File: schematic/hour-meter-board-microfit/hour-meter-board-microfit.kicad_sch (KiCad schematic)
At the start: 0 parts

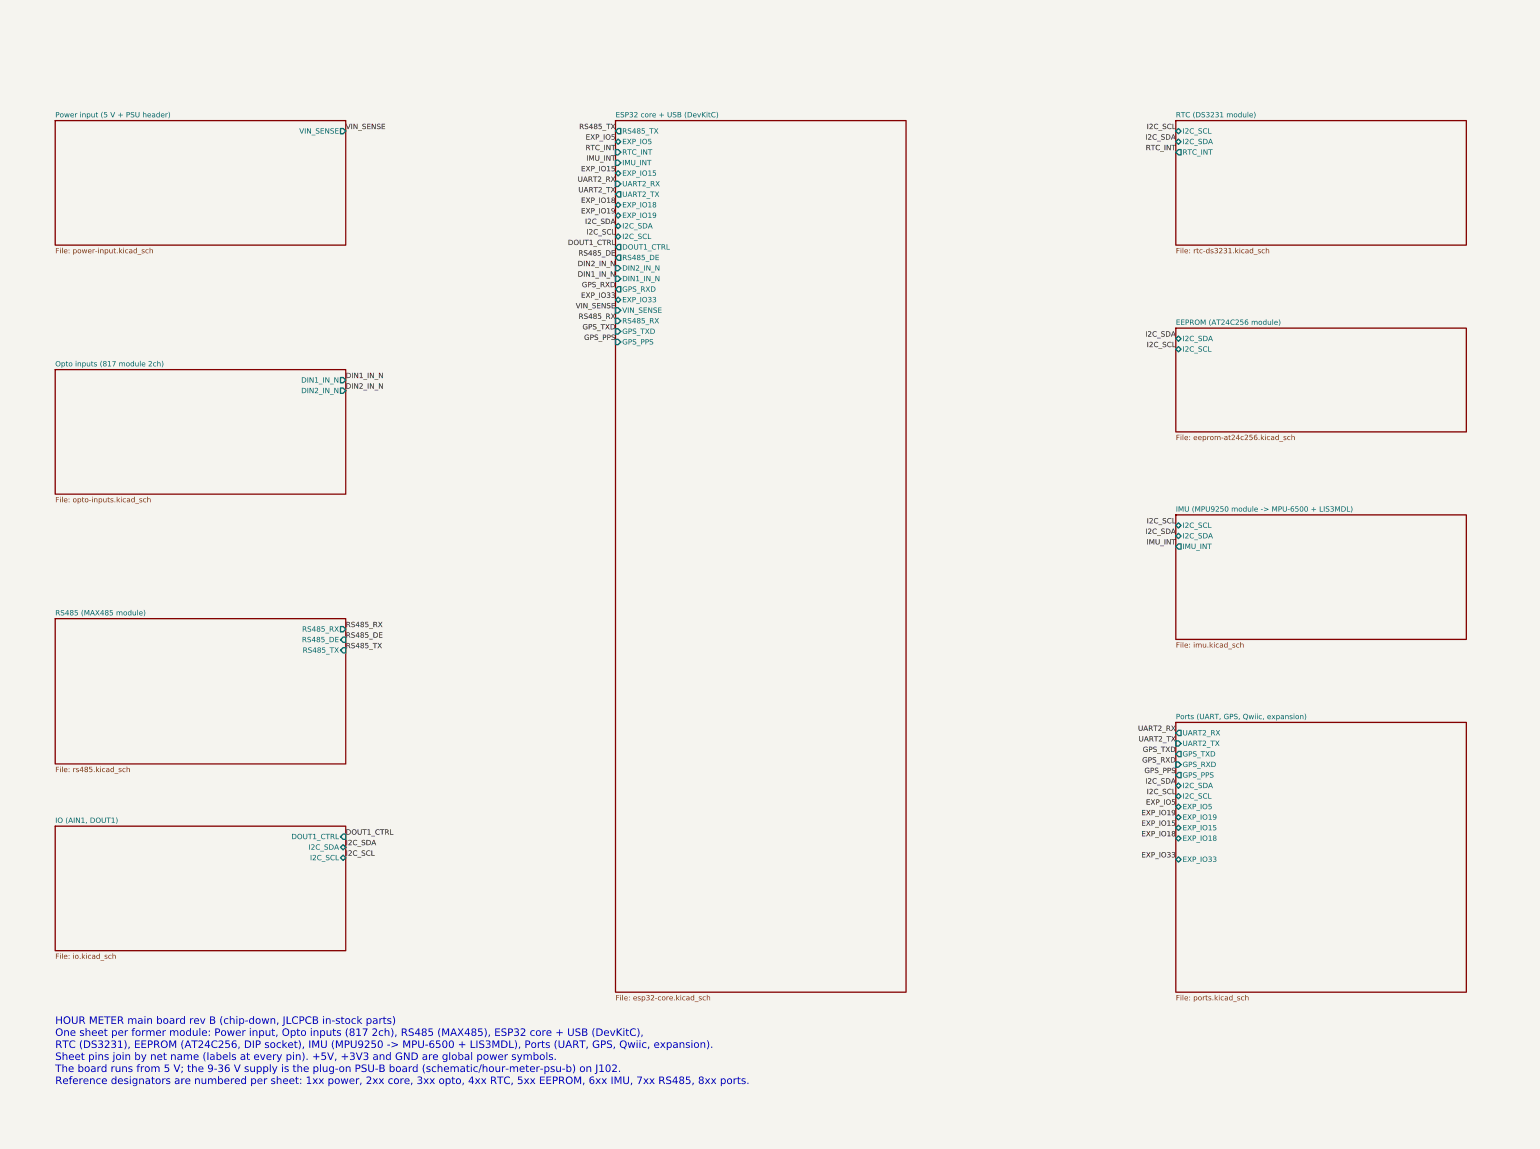
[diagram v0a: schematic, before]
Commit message: feat(pcb): wire the Micro-Fit board's field I/O through one J1 harness
- New Harness sheet: J1 Molex Micro-Fit 3.0 2x7 right-angle header
  (43045-1400, LCSC C277677) replaces J101, J301, J701, J801 and J902.
- Pin order: VIN, AIN1, DOUT1, DIN1 and DIN2 sit on the back row (8-14)
  so their 0.8 mm Vehicle clearance never has to fit between two pads.
  The isolated DIN group (DIN1, DIN2 and two DIN COM pins 6/7) fills
  the pin 7/14 end, next to RS485 A/B, which are rated +/-70 V.
- J802 GPS becomes a JST GH 6-pin in the Pixhawk pinout with I2C;
  PPS moves to the TP801 solder pad.
- The J804 expansion header becomes test pads TP802-TP808; F802 and
  F902 go. J501, J702 and J703 become solder jumpers JP501, JP702-JP704.
- U501 is now the SOIC-8 AT24C256C-SSHL-T (C6482); TP101/TP102 dropped.
- Net-class patterns follow the renamed root nets; ERC shows only the
  two known IMU warnings.
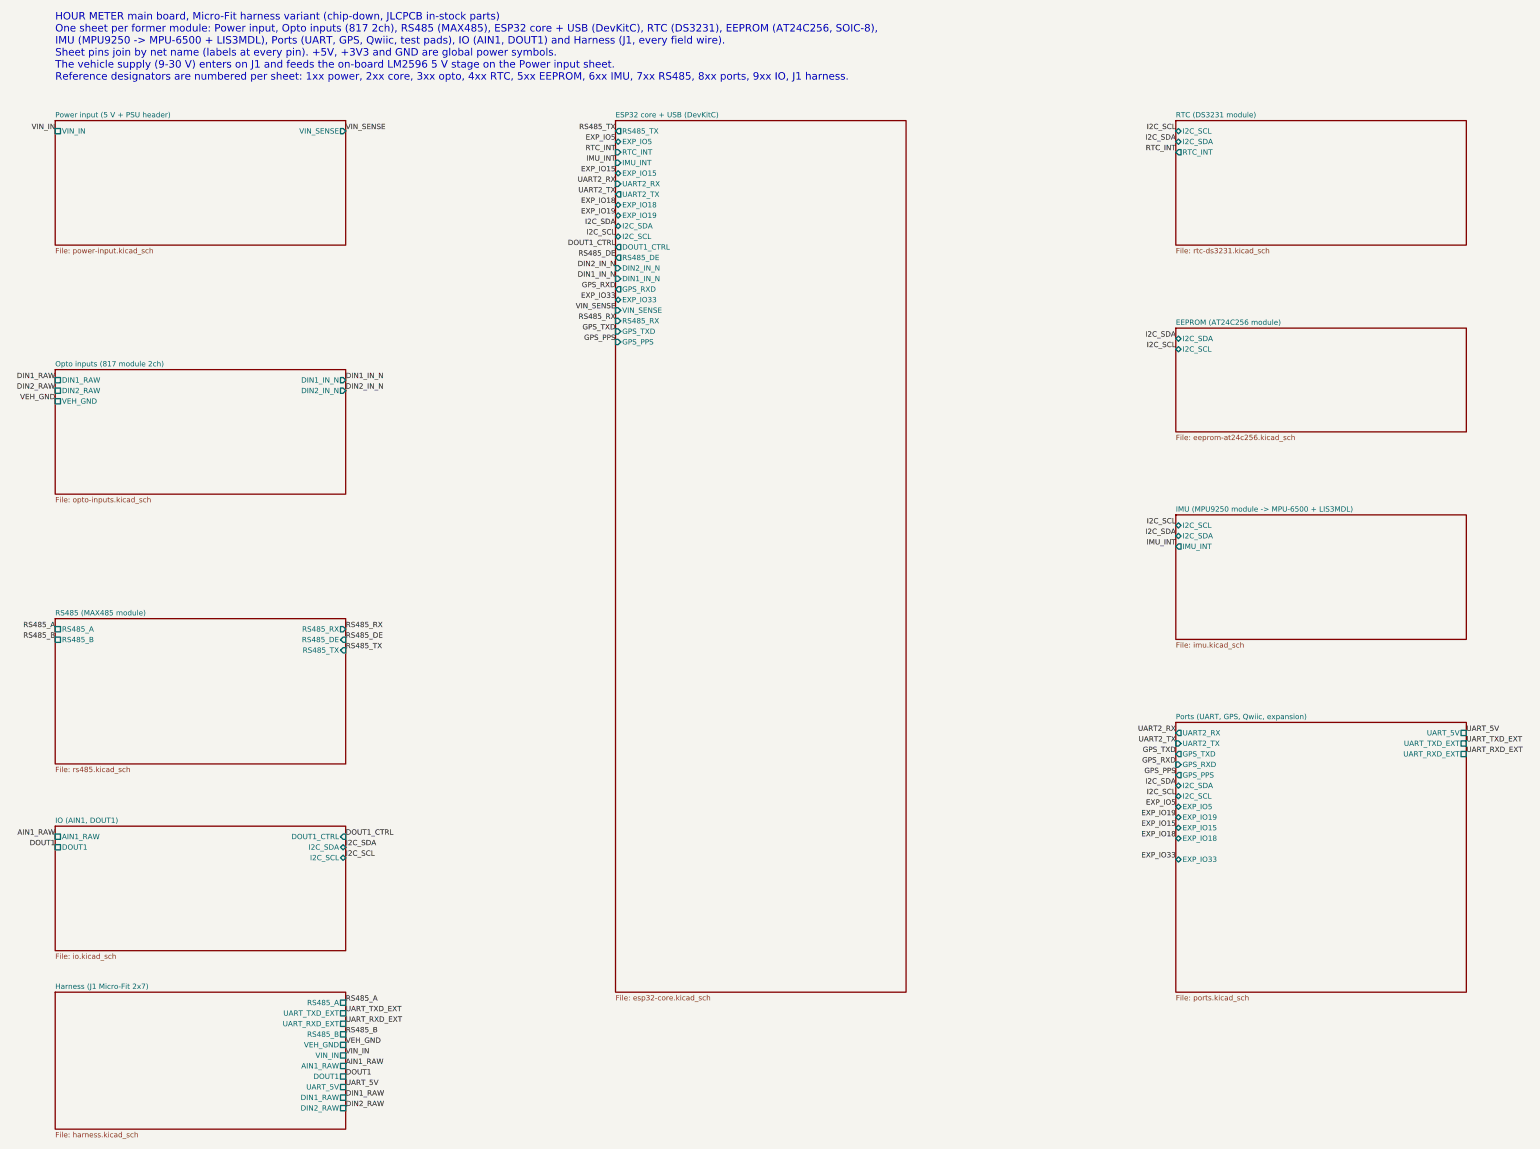
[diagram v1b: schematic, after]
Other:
- added sheet Harness (J1 Micro-Fit 2x7) (harness.kicad_sch)
- sheet IO (AIN1, DOUT1) ports: added AIN1_RAW, DOUT1; removed none
- sheet Opto inputs (817 module 2ch) ports: added DIN1_RAW, DIN2_RAW, VEH_GND; removed none
- sheet Ports (UART, GPS, Qwiic, expansion) ports: added UART_5V, UART_RXD_EXT, UART_TXD_EXT; removed none
- sheet Power input (5 V + PSU header) ports: added VIN_IN; removed none
- sheet RS485 (MAX485 module) ports: added RS485_A, RS485_B; removed none
- note added: "HOUR METER main board, Micro-Fit harness variant (chip-down, JLCPCB in-stock parts) One sheet per former module: Power input, Opto inputs (817 2ch), RS485 (MAX485), ESP32 core + USB (DevKitC), RTC (DS3231), EEPROM (AT24C256, SOIC-8), IMU (MPU9250 -> MPU-6500 + LIS3MDL), Ports (UART, GPS, Qwiic, test pads), IO (AIN1, DOUT1) and Harness (J1, every field wire). Sheet pins join by net name (labels at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"
- note removed: "HOUR METER main board rev B (chip-down, JLCPCB in-stock parts) One sheet per former module: Power input, Opto inputs (817 2ch), RS485 (MAX485), ESP32 core + USB (DevKitC), RTC (DS3231), EEPROM (AT24C256, DIP socket), IMU (MPU9250 -> MPU-6500 + LIS3MDL), Ports (UART, GPS, Qwiic, expansion). Sheet pins join by net name (labels at every pin). +5V, +3V3 and GND are global power symbols. The board run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"
